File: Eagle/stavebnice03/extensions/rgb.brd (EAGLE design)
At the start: 6 parts

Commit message: minor element position changes
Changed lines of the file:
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@@
 <layer number="17" name="Pads" color="2" fill="1" visible="yes" active="yes"/>
 <layer number="18" name="Vias" color="2" fill="1" visible="yes" active="yes"/>
-<layer number="19" name="Unrouted" color="6" fill="1" visible="yes" active="yes"/>
+<layer number="19" name="Unrouted" color="6" fill="1" visible="no" active="yes"/>
 <layer number="20" name="Dimension" color="15" fill="1" visible="yes" active="yes"/>
-<layer number="21" name="tPlace" color="7" fill="1" visible="yes" active="yes"/>
-<layer number="22" name="bPlace" color="7" fill="1" visible="yes" active="yes"/>
-<layer number="23" name="tOrigins" color="15" fill="1" visible="yes" active="yes"/>
+<layer number="21" name="tPlace" color="7" fill="1" visible="no" active="yes"/>
+<layer number="22" name="bPlace" color="7" fill="1" visible="no" active="yes"/>
+<layer number="23" name="tOrigins" color="15" fill="1" visible="no" active="yes"/>
 <layer number="24" name="bOrigins" color="15" fill="1" visible="no" active="yes"/>
 <layer number="25" name="tNames" color="7" fill="1" visible="no" active="yes"/>
@@
 <layer number="42" name="bRestrict" color="1" fill="10" visible="no" active="yes"/>
 <layer number="43" name="vRestrict" color="2" fill="10" visible="no" active="yes"/>
-<layer number="44" name="Drills" color="7" fill="1" visible="yes" active="yes"/>
-<layer number="45" name="Holes" color="7" fill="1" visible="yes" active="yes"/>
+<layer number="44" name="Drills" color="7" fill="1" visible="no" active="yes"/>
+<layer number="45" name="Holes" color="7" fill="1" visible="no" active="yes"/>
 <layer number="46" name="Milling" color="3" fill="1" visible="no" active="yes"/>
 <layer number="47" name="Measures" color="7" fill="1" visible="no" active="yes"/>
-<layer number="48" name="Document" color="7" fill="1" visible="yes" active="yes"/>
+<layer number="48" name="Document" color="7" fill="1" visible="no" active="yes"/>
 <layer number="49" name="Reference" color="7" fill="1" visible="yes" active="yes"/>
 <layer number="51" name="tDocu" color="7" fill="1" visible="no" active="yes"/>
@@
 <text x="4.92125" y="-6.0325" size="2.54" layer="16" rot="MR0" align="center">II=I+I</text>
 <text x="4.92125" y="-6.0325" size="2.54" layer="1" align="center">II=I+I</text>
-<text x="10.415" y="29.005" size="1.778" layer="20" align="center">rgb extension</text>
-<wire x1="-2" y1="-2" x2="23" y2="-2" width="0.05" layer="49"/>
-<wire x1="23" y1="-2" x2="23" y2="23" width="0.05" layer="49"/>
-<wire x1="23" y1="23" x2="-2" y2="23" width="0.05" layer="49"/>
-<wire x1="-2" y1="23" x2="-2" y2="-2" width="0.05" layer="49"/>
+<text x="10.5" y="27" size="1.778" layer="20" align="center">rgb extension</text>
+<wire x1="-10" y1="-10" x2="31" y2="-10" width="0.01" layer="49"/>
+<wire x1="31" y1="-10" x2="31" y2="31" width="0.01" layer="49"/>
+<wire x1="31" y1="31" x2="-10" y2="31" width="0.01" layer="49"/>
+<wire x1="-10" y1="31" x2="-10" y2="-10" width="0.01" layer="49"/>
+<circle x="2.2" y="18.8" radius="0.6" width="0.9" layer="116"/>
+<circle x="18.8" y="2.2" radius="0.6" width="0.9" layer="116"/>
+<circle x="19.65" y="19.7" radius="0.329" width="0.357" layer="116"/>
+<circle x="17.11" y="19.7" radius="0.329" width="0.357" layer="116"/>
+<circle x="14.57" y="19.7" radius="0.329" width="0.357" layer="116"/>
+<circle x="12.03" y="19.7" radius="0.329" width="0.357" layer="116"/>
+<circle x="9.49" y="19.7" radius="0.329" width="0.357" layer="116"/>
+<circle x="6.95" y="19.7" radius="0.329" width="0.357" layer="116"/>
+<circle x="1.29" y="1.3" radius="0.329" width="0.357" layer="116"/>
+<circle x="3.83" y="1.3" radius="0.329" width="0.357" layer="116"/>
+<circle x="6.37" y="1.3" radius="0.329" width="0.357" layer="116"/>
+<circle x="8.91" y="1.3" radius="0.329" width="0.357" layer="116"/>
 </plain>
 <attributes>

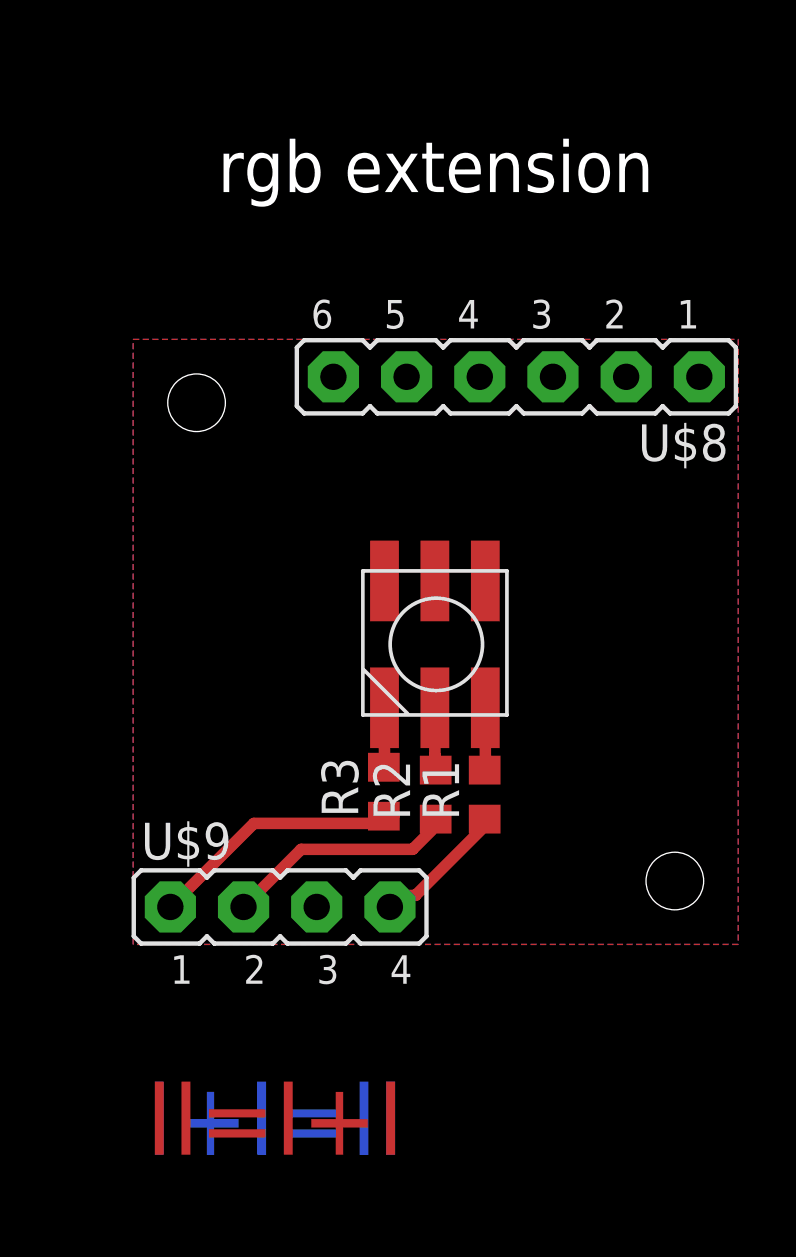
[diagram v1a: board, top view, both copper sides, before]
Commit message: fix of bugs on rgb and lipol board + a few minor changes
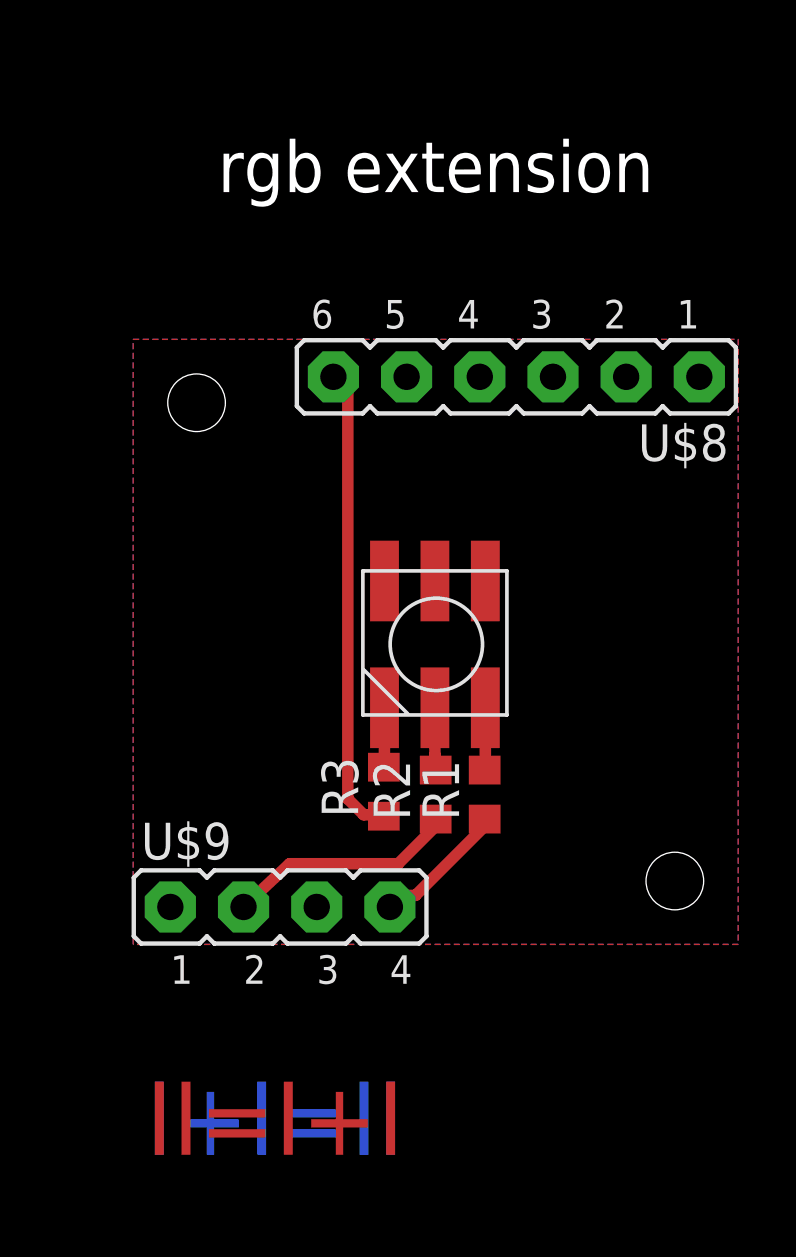
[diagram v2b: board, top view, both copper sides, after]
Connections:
- net N$6: now also U$8.6; no longer U$9.1
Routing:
- net N$6: track 9.41 -> 16.4 mm
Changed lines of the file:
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@@
 <setting verticaltext="up"/>
 </settings>
-<grid distance="0.5" unitdist="mm" unit="mm" style="lines" multiple="1" display="no" altdistance="0.025" altunitdist="inch" altunit="inch"/>
+<grid distance="0.1" unitdist="mm" unit="mm" style="lines" multiple="1" display="no" altdistance="0.025" altunitdist="inch" altunit="inch"/>
 <layers>
 <layer number="1" name="Top" color="4" fill="1" visible="yes" active="yes"/>
@@
 <layer number="17" name="Pads" color="2" fill="1" visible="yes" active="yes"/>
 <layer number="18" name="Vias" color="2" fill="1" visible="yes" active="yes"/>
-<layer number="19" name="Unrouted" color="6" fill="1" visible="no" active="yes"/>
+<layer number="19" name="Unrouted" color="6" fill="1" visible="yes" active="yes"/>
 <layer number="20" name="Dimension" color="15" fill="1" visible="yes" active="yes"/>
 <layer number="21" name="tPlace" color="7" fill="1" visible="no" active="yes"/>
@@
 <signals>
 <signal name="GND">
-<polygon width="0.01" layer="1" isolate="0.4826" thermals="no" rank="2">
+<polygon width="0.01" layer="1" isolate="0.4826" orphans="yes" thermals="no" rank="2">
 <vertex x="0" y="0"/>
 <vertex x="0" y="21"/>
@@
 <contactref element="U$9" pad="2"/>
 <wire x1="10.5" y1="4.35" x2="10.5" y2="4.1" width="0.4" layer="1"/>
-<wire x1="10.5" y1="4.1" x2="9.7" y2="3.3" width="0.4" layer="1"/>
-<wire x1="9.7" y1="3.3" x2="5.83" y2="3.3" width="0.4" layer="1"/>
-<wire x1="5.83" y1="3.3" x2="3.83" y2="1.3" width="0.4" layer="1"/>
+<wire x1="10.5" y1="4.1" x2="9.2" y2="2.8" width="0.4" layer="1"/>
+<wire x1="9.2" y1="2.8" x2="5.43" y2="2.8" width="0.4" layer="1"/>
+<wire x1="5.43" y1="2.8" x2="3.83" y2="1.3" width="0.4" layer="1"/>
 </signal>
 <signal name="N$6">
 <contactref element="R3" pad="1"/>
-<contactref element="U$9" pad="1"/>
-<wire x1="8.7" y1="4.45" x2="9.05" y2="4.45" width="0.4" layer="1"/>
-<wire x1="9.05" y1="4.45" x2="8.8" y2="4.2" width="0.4" layer="1"/>
-<wire x1="8.8" y1="4.2" x2="4.19" y2="4.2" width="0.4" layer="1"/>
-<wire x1="4.19" y1="4.2" x2="1.29" y2="1.3" width="0.4" layer="1"/>
+<contactref element="U$8" pad="6"/>
+<wire x1="7.45" y1="5.05" x2="8" y2="4.5" width="0.4" layer="1"/>
+<wire x1="8" y1="4.5" x2="8.65" y2="4.5" width="0.4" layer="1"/>
+<wire x1="8.65" y1="4.5" x2="8.7" y2="4.45" width="0.4" layer="1"/>
+<wire x1="7.45" y1="5.05" x2="7.45" y2="19.2" width="0.4" layer="1"/>
+<wire x1="7.45" y1="19.2" x2="6.95" y2="19.7" width="0.4" layer="1"/>
 </signal>
 </signals>

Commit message: eagle adjustment for the Jíťa version
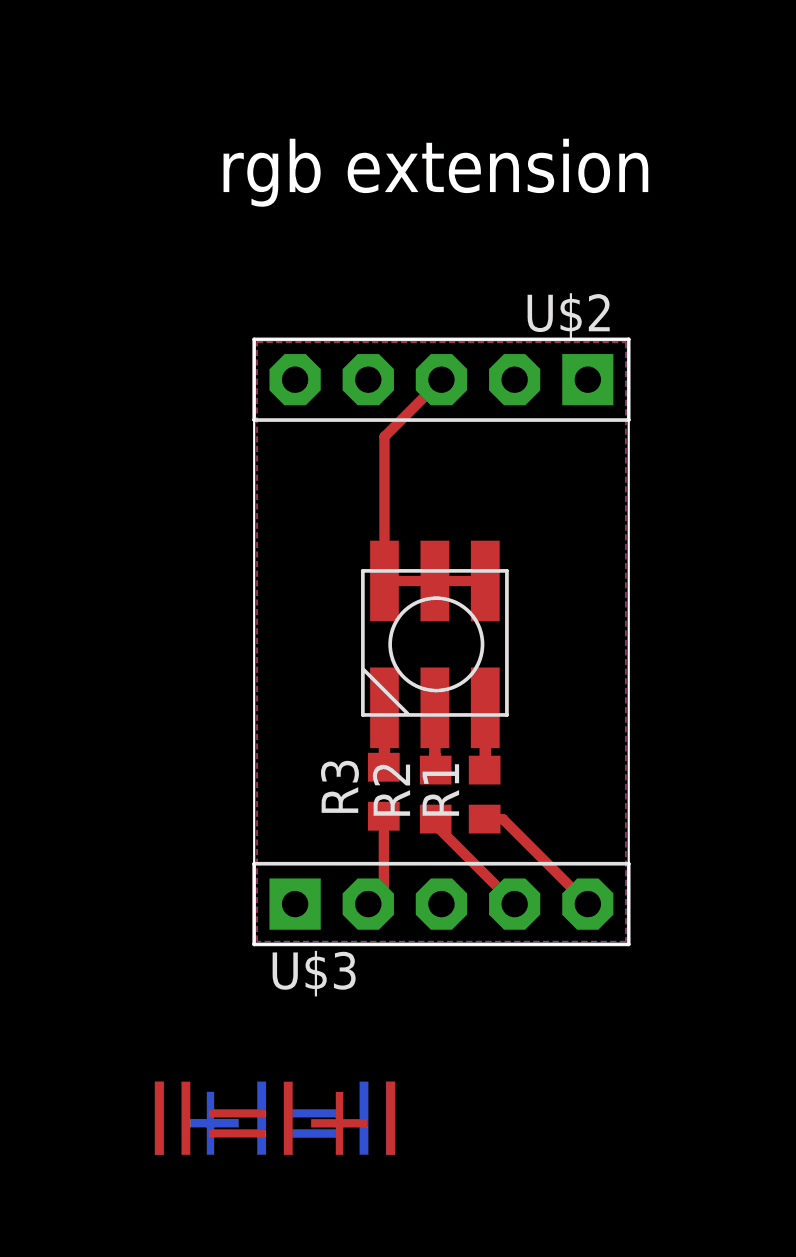
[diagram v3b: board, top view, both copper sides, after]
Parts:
- removed U$8: JUMPER6M, !stavebnice03:JUMPER6M
- removed U$9: JUMPER4M, !stavebnice03:JUMPER4M
- added U$2, U$3: JUMPER5M, !stavebnice03:JUMPER5M
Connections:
- net GND: now also U$2.3; no longer U$8.3
- net N$1: now also R3.1, U$3.2; no longer R1.1, U$9.4
- net N$5: now also U$3.4; no longer U$9.2
- net N$6: now also R1.1, U$3.5; no longer R3.1, U$8.6
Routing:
- net N$6: track 16.4 -> 4.80 mm
- net GND: track 0.00 -> 11.3 mm
- net N$5: track 8.05 -> 4.08 mm
- net N$1: track 4.67 -> 3.27 mm
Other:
- board outline added: 13 x 21 mm
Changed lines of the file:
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@@
 <layers>
 <layer number="1" name="Top" color="4" fill="1" visible="yes" active="yes"/>
-<layer number="16" name="Bottom" color="1" fill="1" visible="no" active="yes"/>
+<layer number="16" name="Bottom" color="1" fill="1" visible="yes" active="yes"/>
 <layer number="17" name="Pads" color="2" fill="1" visible="yes" active="yes"/>
 <layer number="18" name="Vias" color="2" fill="1" visible="yes" active="yes"/>
 <layer number="19" name="Unrouted" color="6" fill="1" visible="yes" active="yes"/>
 <layer number="20" name="Dimension" color="15" fill="1" visible="yes" active="yes"/>
-<layer number="21" name="tPlace" color="7" fill="1" visible="no" active="yes"/>
-<layer number="22" name="bPlace" color="7" fill="1" visible="no" active="yes"/>
-<layer number="23" name="tOrigins" color="15" fill="1" visible="no" active="yes"/>
-<layer number="24" name="bOrigins" color="15" fill="1" visible="no" active="yes"/>
+<layer number="21" name="tPlace" color="7" fill="1" visible="yes" active="yes"/>
+<layer number="22" name="bPlace" color="7" fill="1" visible="yes" active="yes"/>
+<layer number="23" name="tOrigins" color="15" fill="1" visible="yes" active="yes"/>
+<layer number="24" name="bOrigins" color="15" fill="1" visible="yes" active="yes"/>
 <layer number="25" name="tNames" color="7" fill="1" visible="no" active="yes"/>
 <layer number="26" name="bNames" color="7" fill="1" visible="no" active="yes"/>
@@
 <layer number="42" name="bRestrict" color="1" fill="10" visible="no" active="yes"/>
 <layer number="43" name="vRestrict" color="2" fill="10" visible="no" active="yes"/>
-<layer number="44" name="Drills" color="7" fill="1" visible="no" active="yes"/>
-<layer number="45" name="Holes" color="7" fill="1" visible="no" active="yes"/>
+<layer number="44" name="Drills" color="7" fill="1" visible="yes" active="yes"/>
+<layer number="45" name="Holes" color="7" fill="1" visible="yes" active="yes"/>
 <layer number="46" name="Milling" color="3" fill="1" visible="no" active="yes"/>
 <layer number="47" name="Measures" color="7" fill="1" visible="no" active="yes"/>
@@
 <board>
 <plain>
-<wire x1="0" y1="0" x2="0" y2="21" width="0.0762" layer="49"/>
-<wire x1="0" y1="21" x2="21" y2="21" width="0.0762" layer="49"/>
-<wire x1="21" y1="21" x2="21" y2="0" width="0.0762" layer="49"/>
-<wire x1="21" y1="0" x2="0" y2="0" width="0.0762" layer="49"/>
-<hole x="2.2" y="18.8" drill="2"/>
-<hole x="18.8" y="2.2" drill="2"/>
+<wire x1="4.2" y1="0" x2="4.2" y2="21" width="0.0762" layer="20"/>
+<wire x1="4.2" y1="21" x2="17.2" y2="21" width="0.0762" layer="20"/>
+<wire x1="17.2" y1="21" x2="17.2" y2="0" width="0.0762" layer="20"/>
+<wire x1="17.2" y1="0" x2="4.2" y2="0" width="0.0762" layer="20"/>
 <text x="4.92125" y="-6.0325" size="2.54" layer="16" rot="MR0" align="center">II=I+I</text>
 <text x="4.92125" y="-6.0325" size="2.54" layer="1" align="center">II=I+I</text>
@@
 <wire x1="31" y1="31" x2="-10" y2="31" width="0.01" layer="49"/>
 <wire x1="-10" y1="31" x2="-10" y2="-10" width="0.01" layer="49"/>
-<circle x="2.2" y="18.8" radius="0.6" width="0.9" layer="116"/>
-<circle x="18.8" y="2.2" radius="0.6" width="0.9" layer="116"/>
-<circle x="19.65" y="19.7" radius="0.329" width="0.357" layer="116"/>
-<circle x="17.11" y="19.7" radius="0.329" width="0.357" layer="116"/>
-<circle x="14.57" y="19.7" radius="0.329" width="0.357" layer="116"/>
-<circle x="12.03" y="19.7" radius="0.329" width="0.357" layer="116"/>
-<circle x="9.49" y="19.7" radius="0.329" width="0.357" layer="116"/>
-<circle x="6.95" y="19.7" radius="0.329" width="0.357" layer="116"/>
-<circle x="1.29" y="1.3" radius="0.329" width="0.357" layer="116"/>
-<circle x="3.83" y="1.3" radius="0.329" width="0.357" layer="116"/>
-<circle x="6.37" y="1.3" radius="0.329" width="0.357" layer="116"/>
-<circle x="8.91" y="1.3" radius="0.329" width="0.357" layer="116"/>
 </plain>
 <attributes>
@@
 </autorouter>
 <elements>
-<element name="U$8" library="!stavebnice03" package="JUMPER6M" value="JUMPER6M" x="13.3" y="19.7" rot="R180"/>
-<element name="U$9" library="!stavebnice03" package="JUMPER4M" value="JUMPER4M" x="5.1" y="1.3"/>
 <element name="U$1" library="!stavebnice03" package="RGB_WW-FCE50TC-Q1" value="RGB_WW-FCE50TC-Q1" x="10.5" y="10.5"/>
 <element name="R1" library="resistor" package="R0603" value="" x="12.2" y="5.2" rot="R90"/>
 <element name="R2" library="resistor" package="R0603" value="" x="10.5" y="5.2" rot="R90"/>
 <element name="R3" library="resistor" package="R0603" value="" x="8.7" y="5.3" rot="R90"/>
+<element name="U$2" library="!stavebnice03" package="JUMPER5M" value="JUMPER5M" x="10.7" y="19.6" rot="R180"/>
+<element name="U$3" library="!stavebnice03" package="JUMPER5M" value="JUMPER5M" x="10.7" y="1.4"/>
 </elements>
 <signals>
 <signal name="GND">
-<polygon width="0.01" layer="1" isolate="0.4826" orphans="yes" thermals="no" rank="2">
-<vertex x="0" y="0"/>
-<vertex x="0" y="21"/>
-<vertex x="21" y="21"/>
-<vertex x="21" y="0"/>
+<polygon width="0.2" layer="1" isolate="0.4064" thermals="no" rank="2">
+<vertex x="4.3" y="0.1"/>
+<vertex x="4.3" y="20.9"/>
+<vertex x="17.1" y="20.9"/>
+<vertex x="17.1" y="0.1"/>
 </polygon>
-<polygon width="0.05" layer="16" isolate="0.4064" thermals="no" rank="2">
-<vertex x="0" y="0"/>
-<vertex x="0" y="21"/>
-<vertex x="21" y="21"/>
-<vertex x="21" y="0"/>
+<polygon width="0.2" layer="16" isolate="0.4064" thermals="no" rank="2">
+<vertex x="4.3" y="0.1"/>
+<vertex x="4.3" y="20.9"/>
+<vertex x="17.1" y="20.9"/>
+<vertex x="17.1" y="0.1"/>
 </polygon>
-<contactref element="U$8" pad="3"/>
 <contactref element="U$1" pad="4"/>
 <contactref element="U$1" pad="5"/>
 <contactref element="U$1" pad="6"/>
+<contactref element="U$2" pad="3"/>
+<wire x1="8.722" y1="12.614" x2="8.722" y2="17.622" width="0.3556" layer="1"/>
+<wire x1="8.722" y1="17.622" x2="10.7" y2="19.6" width="0.3556" layer="1"/>
+<wire x1="8.722" y1="12.614" x2="12.222" y2="12.614" width="0.3556" layer="1"/>
 </signal>
 <signal name="N$19">
@@
 <wire x1="8.722" y1="6.372" x2="8.7" y2="6.15" width="0.4" layer="1"/>
 </signal>
+<signal name="N$6">
+<contactref element="R1" pad="1"/>
+<contactref element="U$3" pad="5"/>
+<wire x1="12.2" y1="4.35" x2="12.83" y2="4.35" width="0.3556" layer="1"/>
+<wire x1="12.83" y1="4.35" x2="15.78" y2="1.4" width="0.3556" layer="1"/>
+</signal>
 <signal name="N$1">
-<contactref element="R1" pad="1"/>
-<contactref element="U$9" pad="4"/>
-<wire x1="12.2" y1="4.35" x2="12.2" y2="4.1" width="0.4" layer="1"/>
-<wire x1="12.2" y1="4.1" x2="9.8" y2="1.7" width="0.4" layer="1"/>
-<wire x1="9.8" y1="1.7" x2="9.41" y2="1.7" width="0.4" layer="1"/>
-<wire x1="9.41" y1="1.7" x2="8.91" y2="1.3" width="0.4" layer="1"/>
+<contactref element="R3" pad="1"/>
+<contactref element="U$3" pad="2"/>
+<wire x1="8.7" y1="4.45" x2="8.7" y2="1.94" width="0.3556" layer="1"/>
+<wire x1="8.7" y1="1.94" x2="8.16" y2="1.4" width="0.3556" layer="1"/>
 </signal>
 <signal name="N$5">
 <contactref element="R2" pad="1"/>
-<contactref element="U$9" pad="2"/>
-<wire x1="10.5" y1="4.35" x2="10.5" y2="4.1" width="0.4" layer="1"/>
-<wire x1="10.5" y1="4.1" x2="9.2" y2="2.8" width="0.4" layer="1"/>
-<wire x1="9.2" y1="2.8" x2="5.43" y2="2.8" width="0.4" layer="1"/>
-<wire x1="5.43" y1="2.8" x2="3.83" y2="1.3" width="0.4" layer="1"/>
-</signal>
-<signal name="N$6">
-<contactref element="R3" pad="1"/>
-<contactref element="U$8" pad="6"/>
-<wire x1="7.45" y1="5.05" x2="8" y2="4.5" width="0.4" layer="1"/>
-<wire x1="8" y1="4.5" x2="8.65" y2="4.5" width="0.4" layer="1"/>
-<wire x1="8.65" y1="4.5" x2="8.7" y2="4.45" width="0.4" layer="1"/>
-<wire x1="7.45" y1="5.05" x2="7.45" y2="19.2" width="0.4" layer="1"/>
-<wire x1="7.45" y1="19.2" x2="6.95" y2="19.7" width="0.4" layer="1"/>
+<contactref element="U$3" pad="4"/>
+<wire x1="10.5" y1="4.35" x2="10.5" y2="4.14" width="0.3556" layer="1"/>
+<wire x1="10.5" y1="4.14" x2="13.24" y2="1.4" width="0.3556" layer="1"/>
 </signal>
 </signals>
